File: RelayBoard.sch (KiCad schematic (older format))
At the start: 129 parts, among them P1 HE10-32, Q1 NPN, Q10 NPN, Q11 NPN, Q12 NPN, Q13 NPN, Q14 NPN, Q15 NPN, Q16 NPN, Q17 NPN, Q18 NPN, Q19 NPN, Q2 NPN, Q20 NPN, Q21 NPN, Q22 NPN, Q23 NPN, Q24 NPN, Q25 NPN, Q26 NPN, Q27 NPN, Q28 NPN, Q29 NPN, Q3 NPN, Q30 NPN, Q31 NPN, Q32 NPN, Q4 NPN, Q5 NPN, Q6 NPN, Q7 NPN, Q8 NPN, Q9 NPN

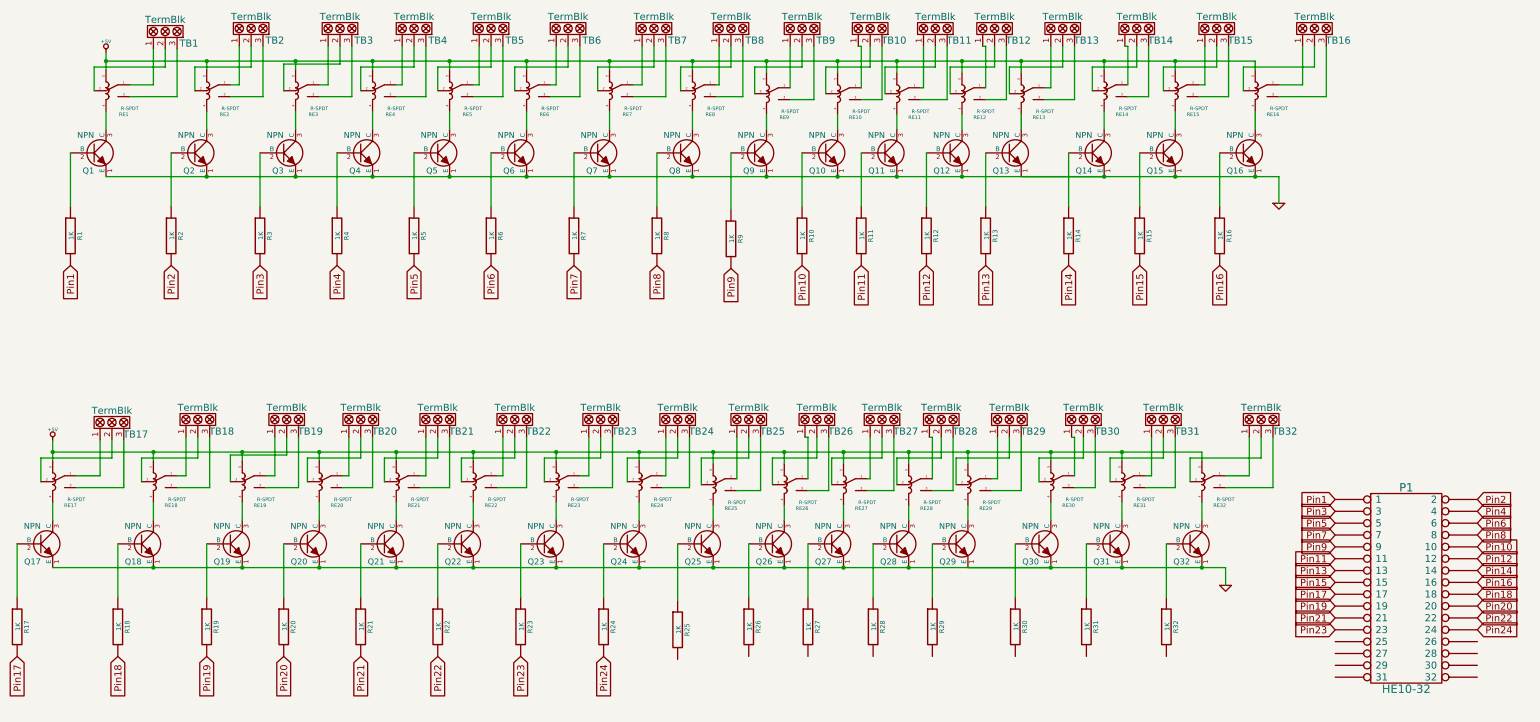
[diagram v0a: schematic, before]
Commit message: Connected Pins 24 to 32, Still need to resolve electric rules errors
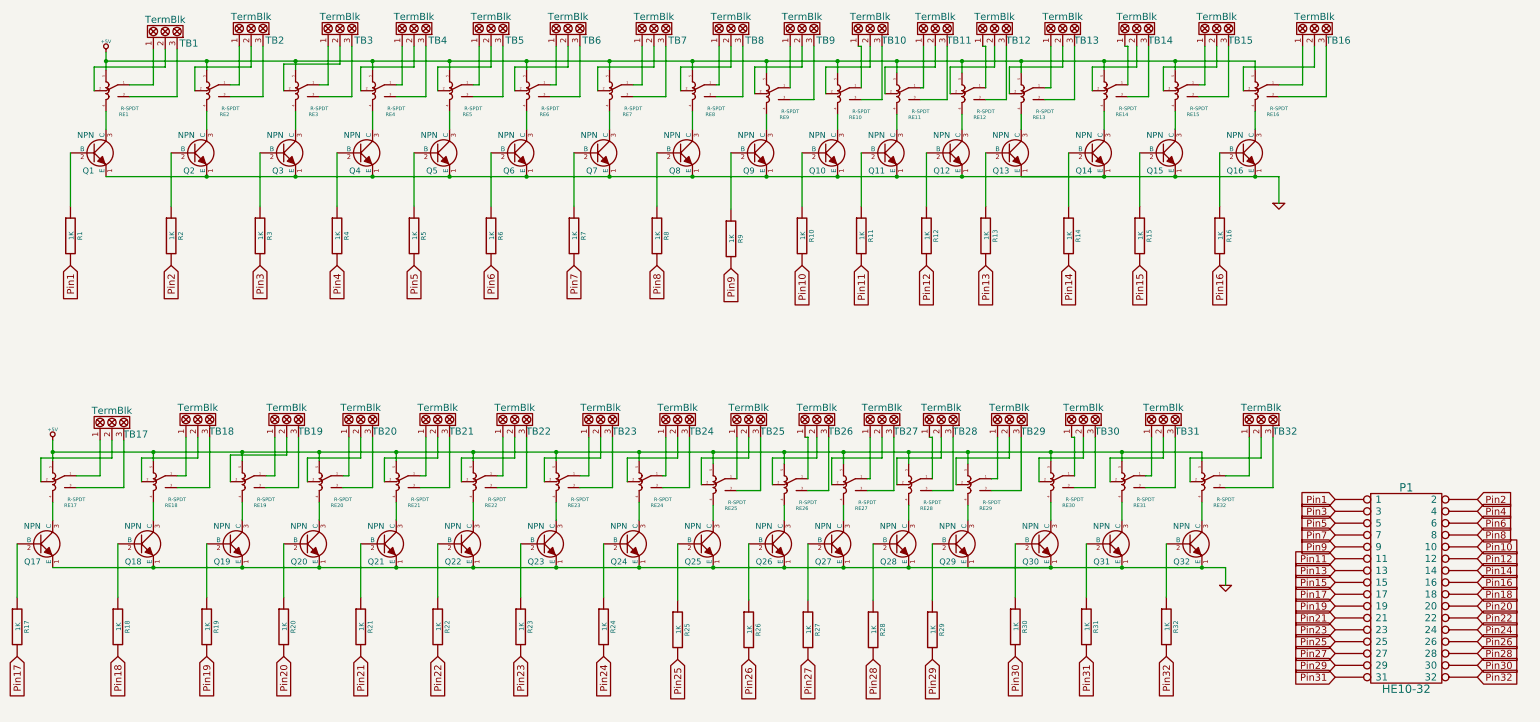
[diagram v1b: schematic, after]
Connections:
- net Pin25: now reaches P1.25
- net Pin25: now also R25.2
- net Pin26: now reaches P1.26
- net Pin26: now also R26.2
- net Pin27: now reaches P1.27
- net Pin27: now also R27.2
- net Pin28: now reaches P1.28
- net Pin28: now also R28.2
- net Pin29: now reaches P1.29
- net Pin29: now also R29.2
- net Pin30: now reaches P1.30
- net Pin30: now also R30.2
- net Pin31: now reaches P1.31
- net Pin31: now also R31.2
- net Pin32: now reaches P1.32
- net Pin32: now also R32.2
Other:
- moved on the sheet: R26, R27, R28, R29
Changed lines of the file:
@@
 	10375 1150 10375 1225
 Connection ~ 9775 1150
-Wire Wire Line
-	11050 1150 11050 1225
 Connection ~ 10375 1150
 Wire Wire Line
@@
 Wire Wire Line
 	11650 1450 11650 1025
-Wire Wire Line
-	1350 1075 1350 1225
 Text GLabel 3950 2875 3    60   Input ~ 0
 Pin5
@@
 L R R26
 U 1 1 54E37DEA
-P 6775 5925
-F 0 "R26" V 6855 5925 40  0000 C CNN
-F 1 "1K" V 6782 5926 40  0000 C CNN
-F 2 "" V 6705 5925 30  0000 C CNN
-F 3 "" H 6775 5925 30  0000 C CNN
-	1    6775 5925
+P 6775 5950
+F 0 "R26" V 6855 5950 40  0000 C CNN
+F 1 "1K" V 6782 5951 40  0000 C CNN
+F 2 "" V 6705 5950 30  0000 C CNN
+F 3 "" H 6775 5950 30  0000 C CNN
+	1    6775 5950
 	1    0    0    -1
 $EndComp
@@
 L R R27
 U 1 1 54E37DF0
-P 7275 5925
-F 0 "R27" V 7355 5925 40  0000 C CNN
-F 1 "1K" V 7282 5926 40  0000 C CNN
-F 2 "" V 7205 5925 30  0000 C CNN
-F 3 "" H 7275 5925 30  0000 C CNN
-	1    7275 5925
+P 7275 5950
+F 0 "R27" V 7355 5950 40  0000 C CNN
+F 1 "1K" V 7282 5951 40  0000 C CNN
+F 2 "" V 7205 5950 30  0000 C CNN
+F 3 "" H 7275 5950 30  0000 C CNN
+	1    7275 5950
 	1    0    0    -1
 $EndComp
@@
 L R R28
 U 1 1 54E37DF6
-P 7825 5925
-F 0 "R28" V 7905 5925 40  0000 C CNN
-F 1 "1K" V 7832 5926 40  0000 C CNN
-F 2 "" V 7755 5925 30  0000 C CNN
-F 3 "" H 7825 5925 30  0000 C CNN
-	1    7825 5925
+P 7825 5950
+F 0 "R28" V 7905 5950 40  0000 C CNN
+F 1 "1K" V 7832 5951 40  0000 C CNN
+F 2 "" V 7755 5950 30  0000 C CNN
+F 3 "" H 7825 5950 30  0000 C CNN
+	1    7825 5950
 	1    0    0    -1
 $EndComp
@@
 L R R29
 U 1 1 54E37DFC
-P 8325 5925
-F 0 "R29" V 8405 5925 40  0000 C CNN
-F 1 "1K" V 8332 5926 40  0000 C CNN
-F 2 "" V 8255 5925 30  0000 C CNN
-F 3 "" H 8325 5925 30  0000 C CNN
-	1    8325 5925
+P 8325 5950
+F 0 "R29" V 8405 5950 40  0000 C CNN
+F 1 "1K" V 8332 5951 40  0000 C CNN
+F 2 "" V 8255 5950 30  0000 C CNN
+F 3 "" H 8325 5950 30  0000 C CNN
+	1    8325 5950
 	1    0    0    -1
 $EndComp
@@
 	6175 5700 6175 5225
 Wire Wire Line
-	6775 5675 6775 5225
-Wire Wire Line
-	7275 5675 7275 5225
-Wire Wire Line
-	7825 5675 7825 5225
-Wire Wire Line
-	8325 5675 8325 5225
+	6775 5700 6775 5225
+Wire Wire Line
+	7275 5700 7275 5225
+Wire Wire Line
+	7825 5700 7825 5225
+Wire Wire Line
+	8325 5700 8325 5225
 Wire Wire Line
 	9025 5675 9025 5225
@@
 Wire Wire Line
 	11250 2125 11250 2350
-Wire Wire Line
-	10800 5425 10800 5575
 Text GLabel 8275 2875 3    60   Input ~ 0
 Pin12
@@
 Text GLabel 12925 5950 2    60   Input ~ 0
 Pin24
+Text GLabel 6175 6200 3    60   Input ~ 0
+Pin25
+Text GLabel 6775 6200 3    60   Input ~ 0
+Pin26
+Text GLabel 7275 6200 3    60   Input ~ 0
+Pin27
+Text GLabel 7825 6200 3    60   Input ~ 0
+Pin28
+Text GLabel 11725 6050 0    60   Input ~ 0
+Pin25
+Text GLabel 12925 6050 2    60   Input ~ 0
+Pin26
+Text GLabel 11725 6150 0    60   Input ~ 0
+Pin27
+Text GLabel 12925 6150 2    60   Input ~ 0
+Pin28
+Text GLabel 8325 6200 3    60   Input ~ 0
+Pin29
+Text GLabel 9025 6175 3    60   Input ~ 0
+Pin30
+Text GLabel 9625 6175 3    60   Input ~ 0
+Pin31
+Text GLabel 10300 6175 3    60   Input ~ 0
+Pin32
+Text GLabel 11725 6250 0    60   Input ~ 0
+Pin29
+Text GLabel 12925 6250 2    60   Input ~ 0
+Pin30
+Text GLabel 11725 6350 0    60   Input ~ 0
+Pin31
+Text GLabel 12925 6350 2    60   Input ~ 0
+Pin32
+Wire Wire Line
+	10800 5425 10800 5575
+Wire Wire Line
+	11050 1150 11050 1225
+Wire Wire Line
+	1350 1225 1350 1075
 $EndSCHEMATC

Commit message: Finished Schematic
* Updated Relay Lib Componet Descriptions
* Generated A NetList
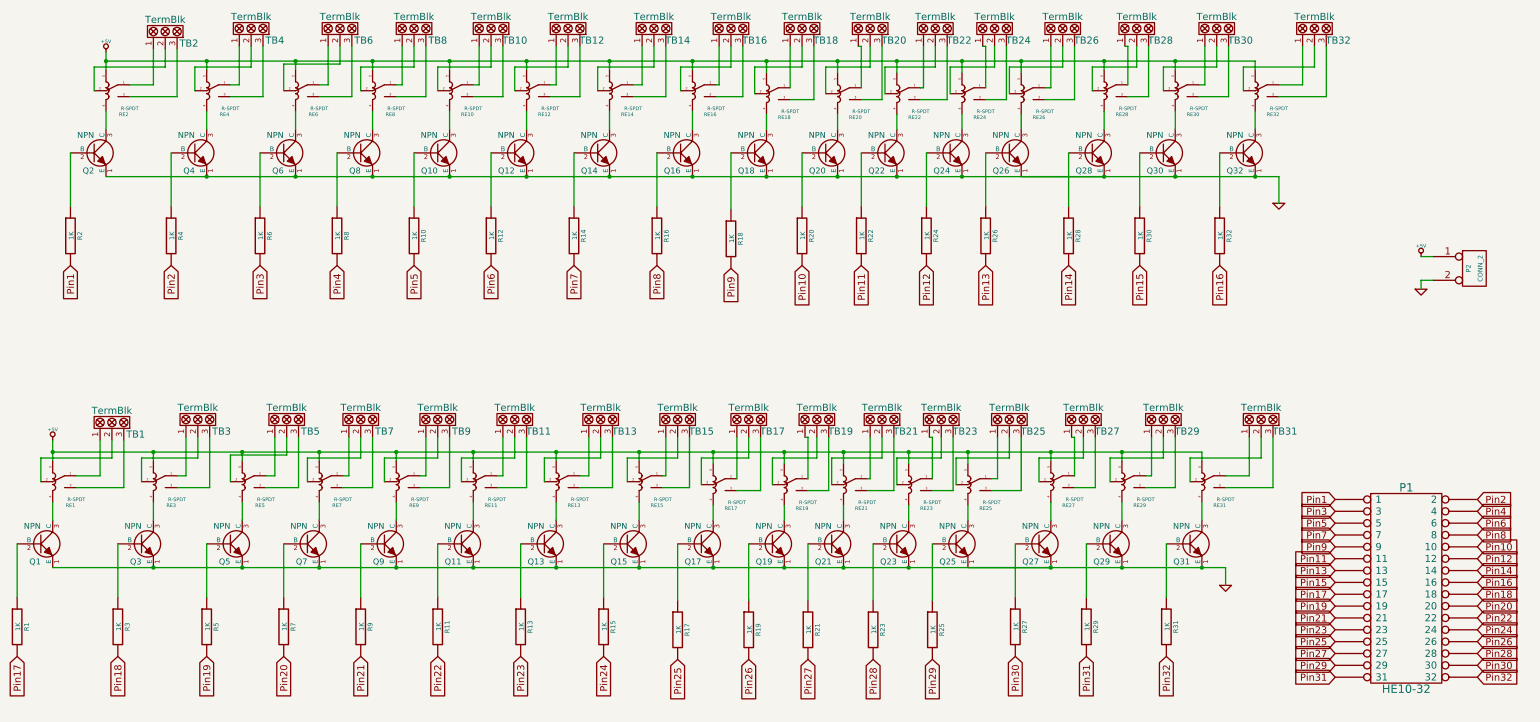
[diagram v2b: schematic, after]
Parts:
- added P2: CONN_2, symbol CONN_2
- renumbered Q17 to Q1, Q5 to Q10, Q22 to Q11, Q6 to Q12, Q23 to Q13, Q7 to Q14, Q24 to Q15, Q8 to Q16, Q25 to Q17, Q9 to Q18, Q26 to Q19, Q1 to Q2, Q10 to Q20, Q27 to Q21, Q11 to Q22, Q28 to Q23, Q12 to Q24, Q29 to Q25, Q13 to Q26, Q30 to Q27, Q14 to Q28, Q31 to Q29, Q18 to Q3, Q15 to Q30, Q32 to Q31, Q16 to Q32, Q2 to Q4, Q19 to Q5, Q3 to Q6, Q20 to Q7, Q4 to Q8, Q21 to Q9, R17 to R1, R5 to R10, R22 to R11, R6 to R12, R23 to R13, R7 to R14, R24 to R15, R8 to R16, R25 to R17, R9 to R18, R26 to R19, R1 to R2, R10 to R20, R27 to R21, R11 to R22, R28 to R23, R12 to R24, R29 to R25, R13 to R26, R30 to R27, R14 to R28, R31 to R29, R18 to R3, R15 to R30, R32 to R31, R16 to R32, R2 to R4, R19 to R5, R3 to R6, R20 to R7, R4 to R8, R21 to R9, RE17 to RE1, RE5 to RE10, RE22 to RE11, RE6 to RE12, RE23 to RE13, RE7 to RE14, RE24 to RE15, RE8 to RE16, RE25 to RE17, RE9 to RE18, RE26 to RE19, RE1 to RE2, RE10 to RE20, RE27 to RE21, RE11 to RE22, RE28 to RE23, RE12 to RE24, RE29 to RE25, RE13 to RE26, RE30 to RE27, RE14 to RE28, RE31 to RE29, RE18 to RE3, RE15 to RE30, RE32 to RE31, RE16 to RE32, RE2 to RE4, RE19 to RE5, RE3 to RE6, RE20 to RE7, RE4 to RE8, RE21 to RE9, TB17 to TB1, TB5 to TB10, TB22 to TB11, TB6 to TB12, TB23 to TB13, TB7 to TB14, TB24 to TB15, TB8 to TB16, TB25 to TB17, TB9 to TB18, TB26 to TB19, TB1 to TB2, TB10 to TB20, TB27 to TB21, TB11 to TB22, TB28 to TB23, TB12 to TB24, TB29 to TB25, TB13 to TB26, TB30 to TB27, TB14 to TB28, TB31 to TB29, TB18 to TB3, TB15 to TB30, TB32 to TB31, TB16 to TB32, TB2 to TB4, TB19 to TB5, TB3 to TB6, TB20 to TB7, TB4 to TB8, TB21 to TB9
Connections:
- net +5V: now also P2.1 (P1)
- net GND: now also P2.2 (PM)

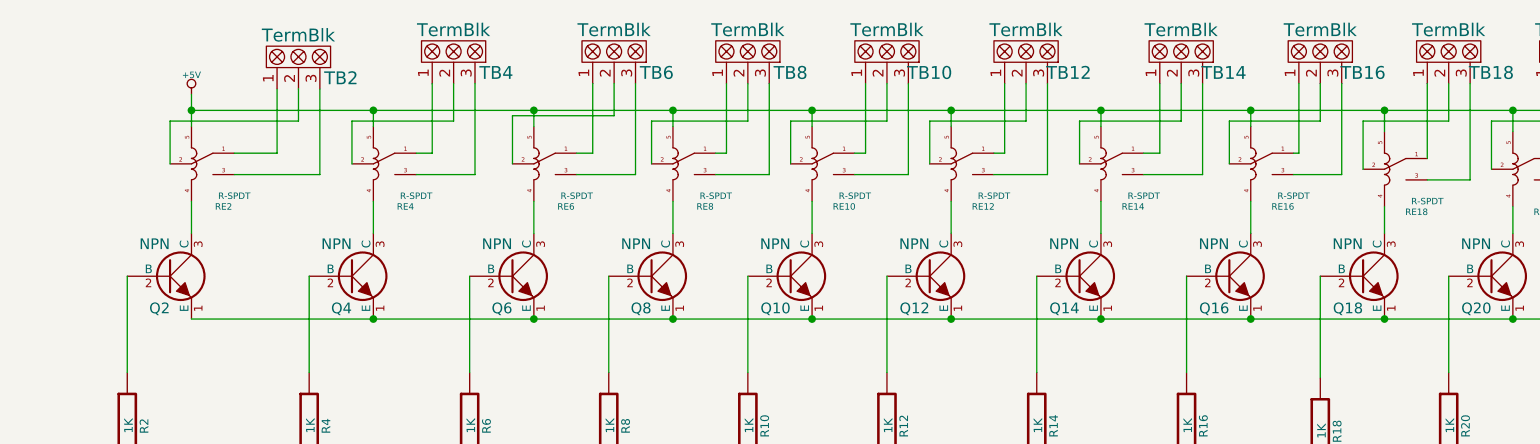
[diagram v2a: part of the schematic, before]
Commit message: Update
* Updated Readme with a warning.
* The schematic is nowhere near done as I forgot to include diodes to
  protect against the feedback from relays turning on and off.
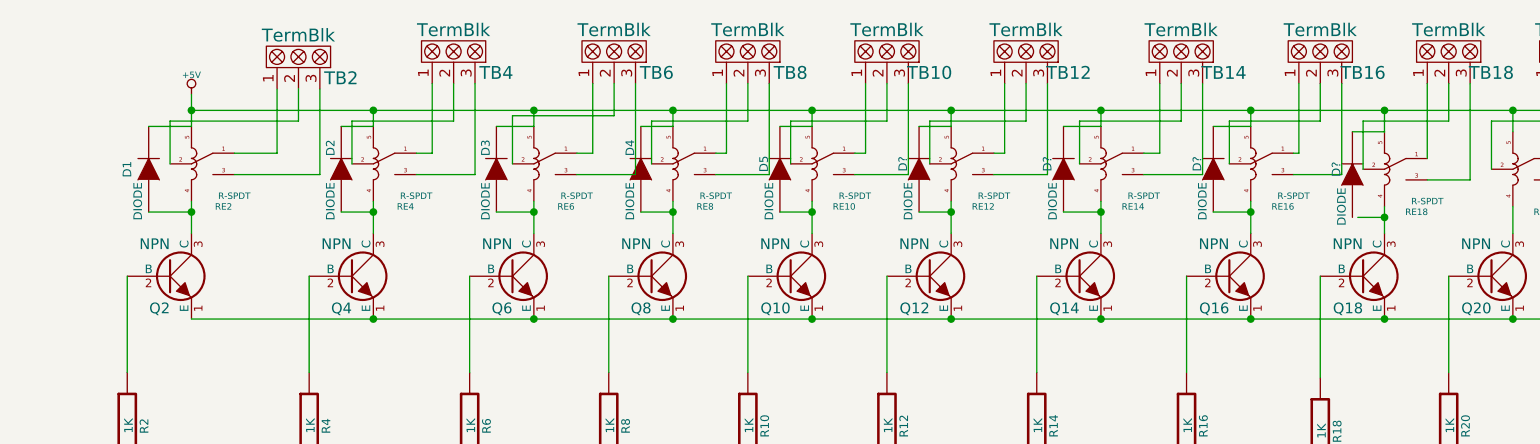
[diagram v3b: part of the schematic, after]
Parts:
- added D1, D2, D3, D4, D5, D? (x4): DIODE, symbol DIODE
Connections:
- net +5V: now also D1.2 (K), D2.2 (K), D3.2 (K), D4.2 (K), D5.2 (K), D?.2 (K), D?.2 (K), D?.2 (K), D?.2 (K)
- net at Q2.3 (C), RE2.4: now also D1.1 (A)
- net at Q4.3 (C), RE4.4: now also D2.1 (A)
- net at Q6.3 (C), RE6.4: now also D3.1 (A)
- net at Q8.3 (C), RE8.4: now also D4.1 (A)
- net at Q10.3 (C), RE10.4: now also D5.1 (A)
- net at Q12.3 (C), RE12.4: now also D?.1 (A)
- net at Q14.3 (C), RE14.4: now also D?.1 (A)
- net at Q16.3 (C), RE16.4: now also D?.1 (A)

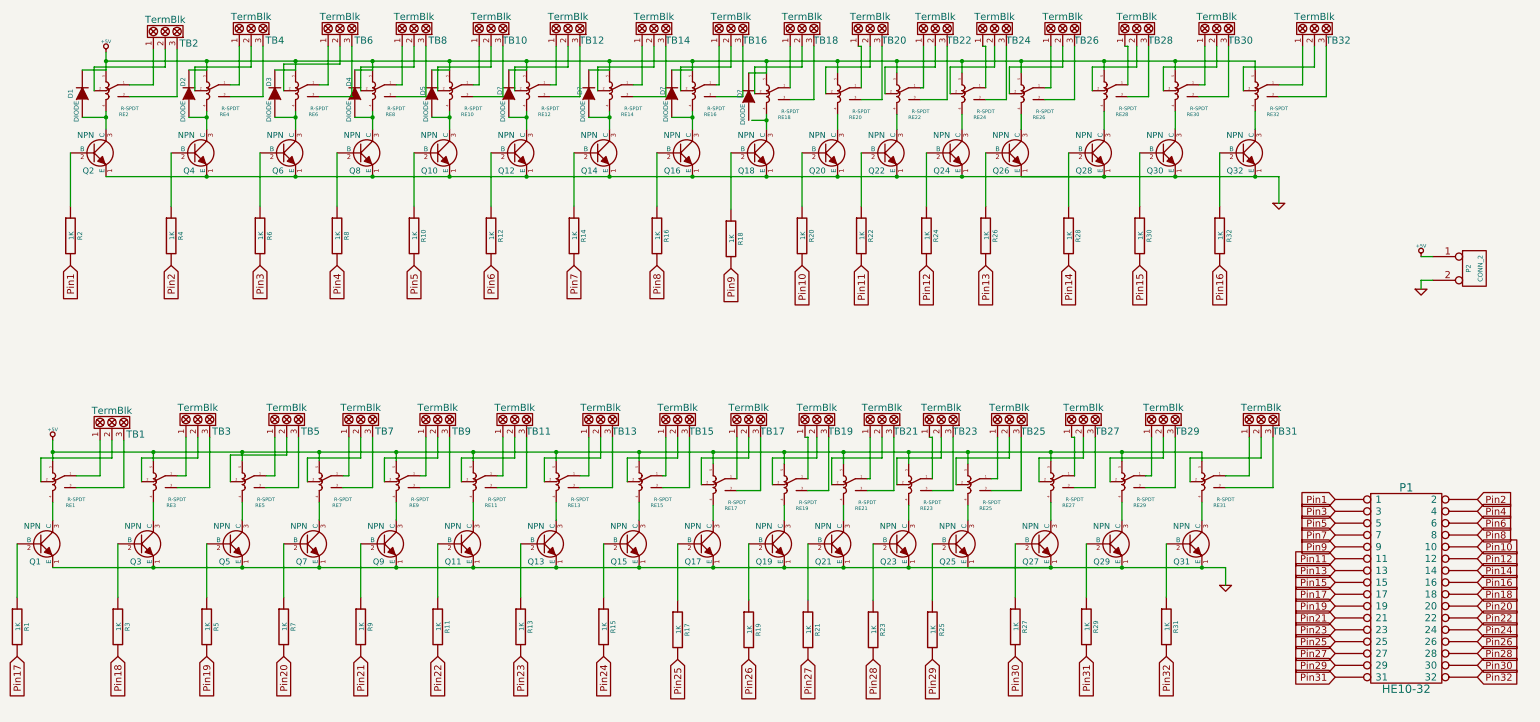
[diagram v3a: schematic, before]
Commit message: Finished Schematic
* The schematic now has diodes where needed
* Parts are associated as needed
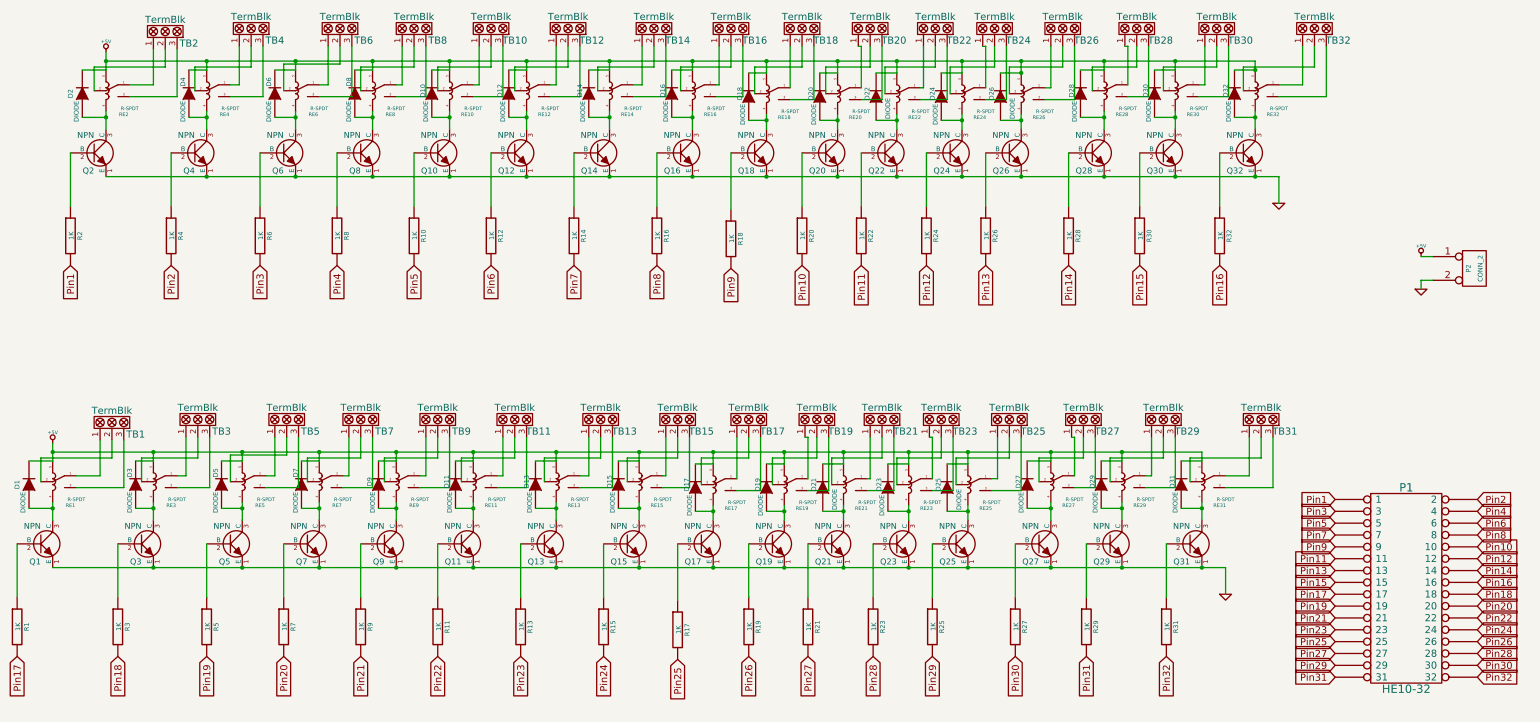
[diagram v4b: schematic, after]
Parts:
- added D1, D11, D13, D15, D17, D19, D20, D21, D22, D23, D24, D25, D26, D27, D28, D29, D3, D30, D31, D32, D5, D7, D9: DIODE, symbol DIODE
- gave numbers to parts that had none: 4
- renumbered D5 to D10, D1 to D2, D2 to D4, D3 to D6, D4 to D8
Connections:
- net +5V: now also D1.2 (K), D11.2 (K), D13.2 (K), D15.2 (K), D17.2 (K), D19.2 (K), D20.2 (K), D21.2 (K), D22.2 (K), D23.2 (K), D24.2 (K), D25.2 (K), D26.2 (K), D27.2 (K), D28.2 (K), D29.2 (K), D3.2 (K), D30.2 (K), D31.2 (K), D32.2 (K), D5.2 (K), D7.2 (K), D9.2 (K)
- net at Q18.3 (C), RE18.4: now also D18.1 (A)
- net at Q20.3 (C), RE20.4: now also D20.1 (A)
- net at Q22.3 (C), RE22.4: now also D22.1 (A)
- net at Q24.3 (C), RE24.4: now also D24.1 (A)
- net at Q26.3 (C), RE26.4: now also D26.1 (A)
- net at Q28.3 (C), RE28.4: now also D28.1 (A)
- net at Q30.3 (C), RE30.4: now also D30.1 (A)
- net at Q32.3 (C), RE32.4: now also D32.1 (A)
- net at Q1.3 (C), RE1.4: now also D1.1 (A)
- net at Q3.3 (C), RE3.4: now also D3.1 (A)
- net at Q5.3 (C), RE5.4: now also D5.1 (A)
- net at Q7.3 (C), RE7.4: now also D7.1 (A)
- net at Q9.3 (C), RE9.4: now also D9.1 (A)
- net at Q11.3 (C), RE11.4: now also D11.1 (A)
- net at Q13.3 (C), RE13.4: now also D13.1 (A)
- net at Q15.3 (C), RE15.4: now also D15.1 (A)
- net at Q17.3 (C), RE17.4: now also D17.1 (A)
- net at Q19.3 (C), RE19.4: now also D19.1 (A)
- net at Q21.3 (C), RE21.4: now also D21.1 (A)
- net at Q23.3 (C), RE23.4: now also D23.1 (A)
- net at Q25.3 (C), RE25.4: now also D25.1 (A)
- net at Q27.3 (C), RE27.4: now also D27.1 (A)
- net at Q29.3 (C), RE29.4: now also D29.1 (A)
- net at Q31.3 (C), RE31.4: now also D31.1 (A)
